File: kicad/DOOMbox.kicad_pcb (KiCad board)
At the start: 2 copper layers, 1 part

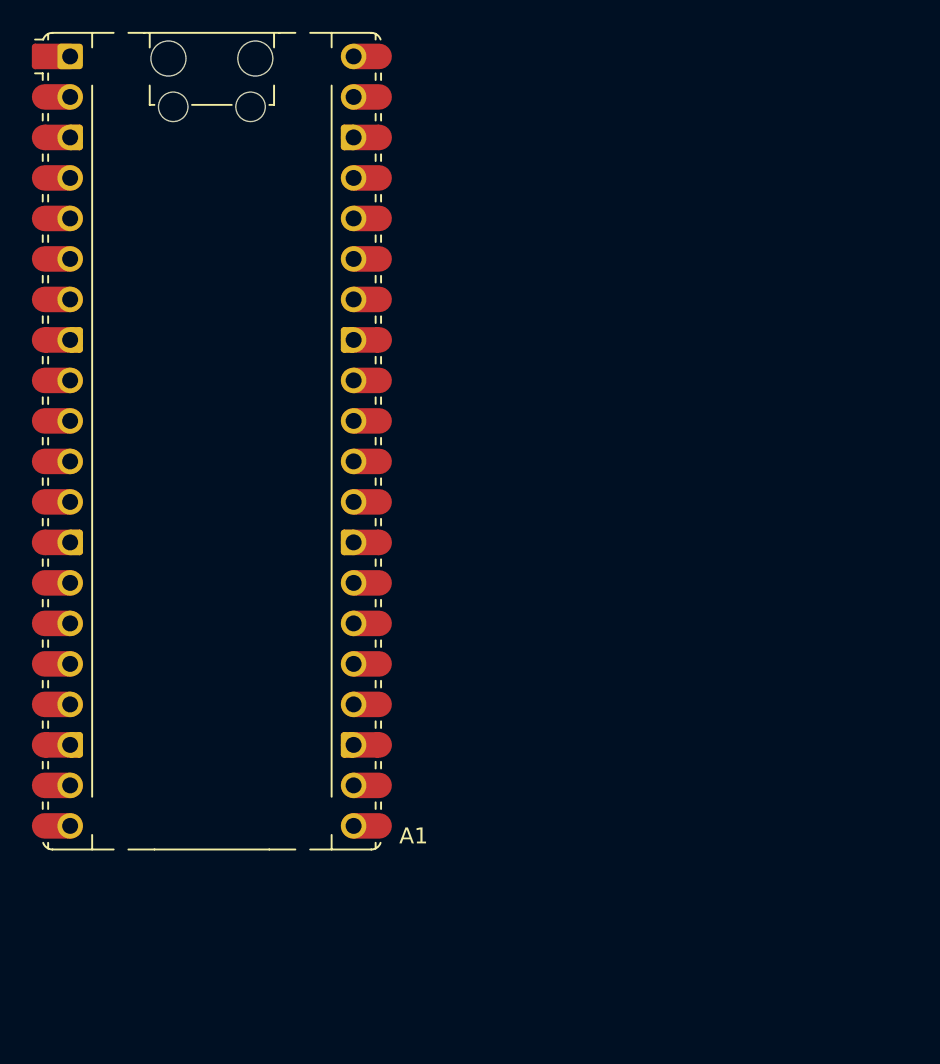
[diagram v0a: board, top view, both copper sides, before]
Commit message: Track necessary KiCad libraries + symbols
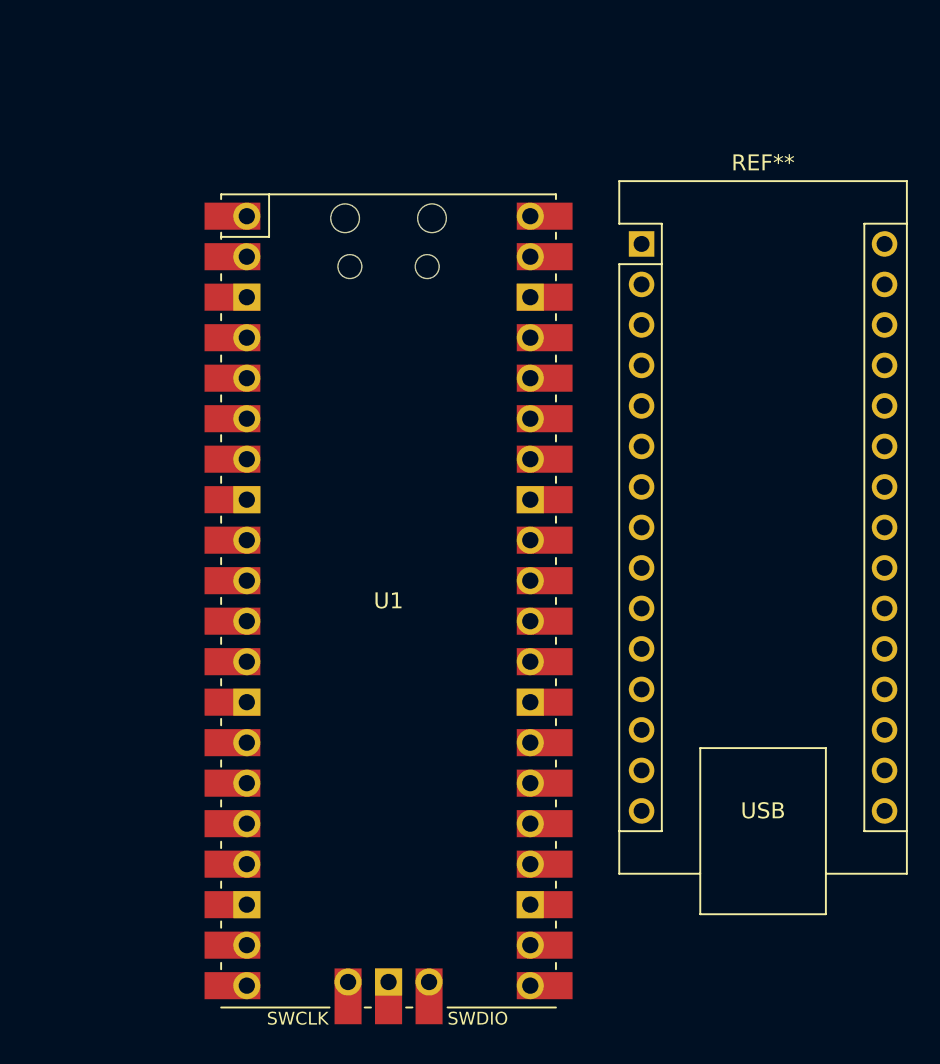
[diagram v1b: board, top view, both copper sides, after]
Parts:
- removed A1: RaspberryPi_Pico_W, Module:RaspberryPi_Pico_Common_Unspecified
- added REF**: Arduino_Nano, Module:Arduino_Nano, F.Cu at (143.8, 72.5)
- added U1: RPi_Pico_SMD_TH, MCU_RPi:RPi_Pico_SMD_TH, F.Cu at (127.9, 94.9)

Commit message: Schematic: add resistor ladder DACs for video data output
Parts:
- removed REF**: Arduino_Nano, Module:Arduino_Nano
- removed U1: RPi_Pico_SMD_TH, MCU_RPi:RPi_Pico_SMD_TH
